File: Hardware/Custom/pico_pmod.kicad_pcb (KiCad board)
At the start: 2 copper layers, 50 x 37 mm, 44 parts, among them J1 Conn_02x06_Odd_Even, J2 Conn_02x06_Odd_Even, J3 Conn_02x06_Odd_Even, J4 USB_C_Receptacle_USB2.0, J5 Conn_01x04, SW1 SW_Push, SW2 SW_Push, U1 RP2040, U2 W25Q128JVS, U3 NCP1117-3.3_SOT223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

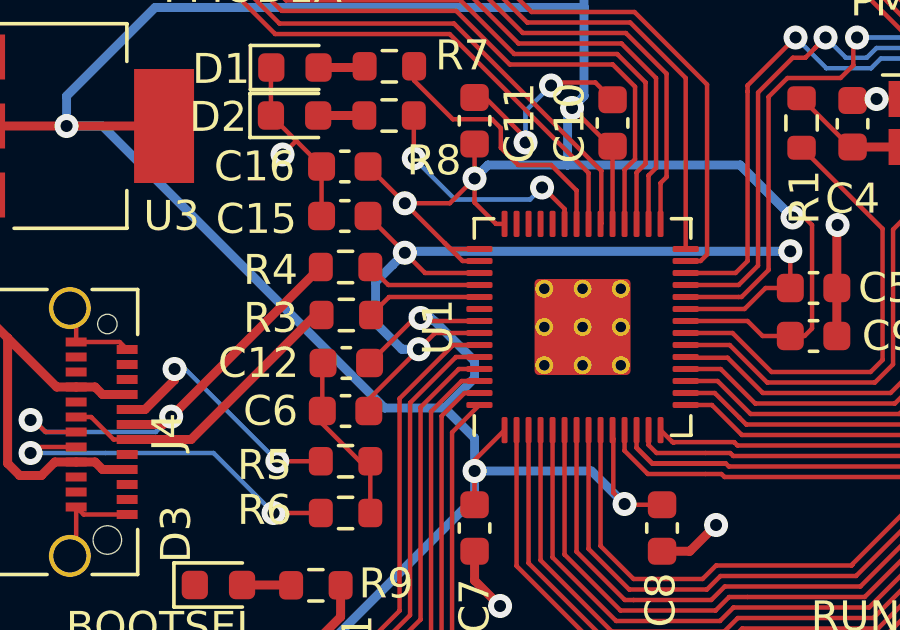
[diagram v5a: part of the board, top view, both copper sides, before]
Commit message: Ensure that pins 48 and 49 are connected to 3v3
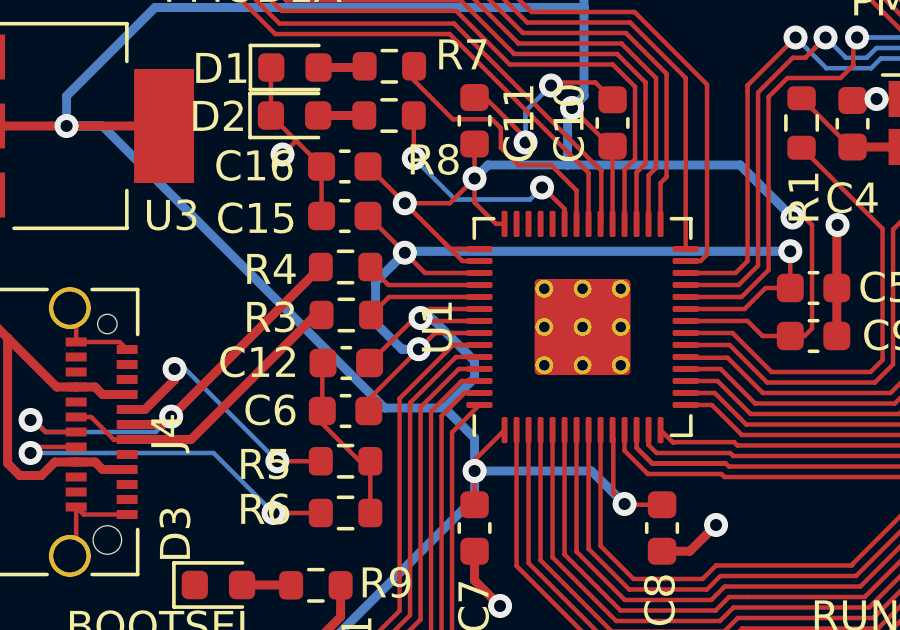
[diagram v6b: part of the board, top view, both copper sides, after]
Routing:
- net +3V3: track 200.0 -> 202.6 mm
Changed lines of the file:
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@@
     (thickness 1.6)
     (drawings 24)
-    (tracks 783)
+    (tracks 787)
     (zones 0)
     (modules 44)
@@
   (page A4)
   (layers
-    (0 F.Cu signal)
+    (0 F.Cu signal hide)
     (31 B.Cu signal)
     (32 B.Adhes user)
@@
   (segment (start 143.175 71.175) (end 144 70.35) (width 0.15) (layer F.Cu) (net 2))
   (segment (start 141.675 71.175) (end 143.175 71.175) (width 0.15) (layer F.Cu) (net 2))
+  (segment (start 142.5 74.7) (end 142.2 75) (width 0.15) (layer F.Cu) (net 2))
+  (segment (start 144.1625 74.7) (end 142.5 74.7) (width 0.15) (layer F.Cu) (net 2))
+  (segment (start 142.55 75) (end 142.65 75.1) (width 0.15) (layer B.Cu) (net 2))
+  (segment (start 142.2 75) (end 142.55 75) (width 0.15) (layer B.Cu) (net 2))
   (segment (start 160.75 67.75) (end 160.7 67.7) (width 0.3) (layer F.Cu) (net 3))
   (segment (start 162.7 67.75) (end 160.75 67.75) (width 0.3) (layer F.Cu) (net 3))

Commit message: update resistor values from schimatic
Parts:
- R7, R8, R9: value R -> 330
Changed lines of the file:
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@@
       (effects (font (size 1 1) (thickness 0.15)))
     )
-    (fp_text value R (at 0 1.43) (layer F.Fab) hide
+    (fp_text value 330 (at 0 1.43) (layer F.Fab) hide
       (effects (font (size 1 1) (thickness 0.15)))
     )
@@
       (effects (font (size 1 1) (thickness 0.15)))
     )
-    (fp_text value R (at 0 1.43) (layer F.Fab) hide
+    (fp_text value 330 (at 0 1.43) (layer F.Fab) hide
       (effects (font (size 1 1) (thickness 0.15)))
     )
@@
       (effects (font (size 1 1) (thickness 0.15)))
     )
-    (fp_text value R (at 0 1.43) (layer F.Fab) hide
+    (fp_text value 330 (at 0 1.43) (layer F.Fab) hide
       (effects (font (size 1 1) (thickness 0.15)))
     )

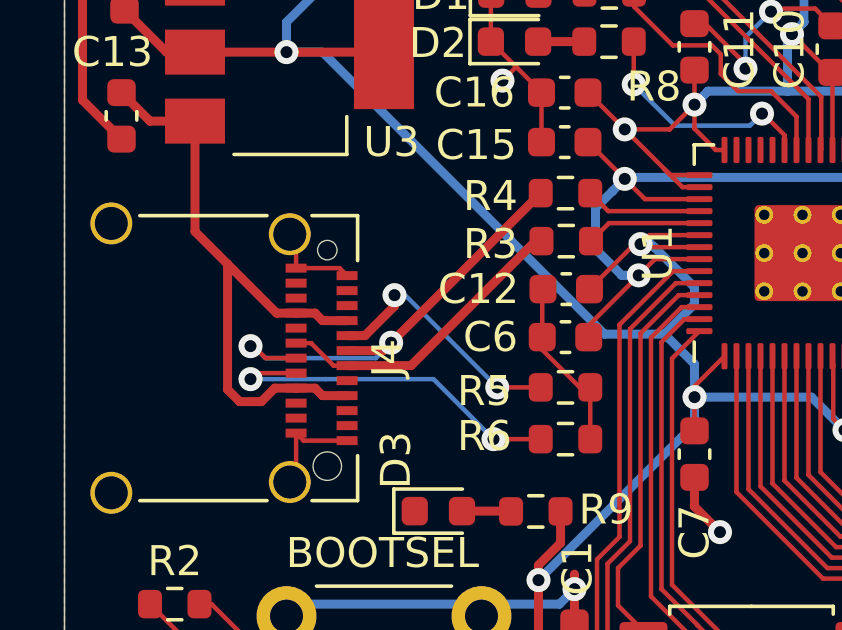
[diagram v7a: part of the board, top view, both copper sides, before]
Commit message: Correct USB DP and DN on PCB for #7
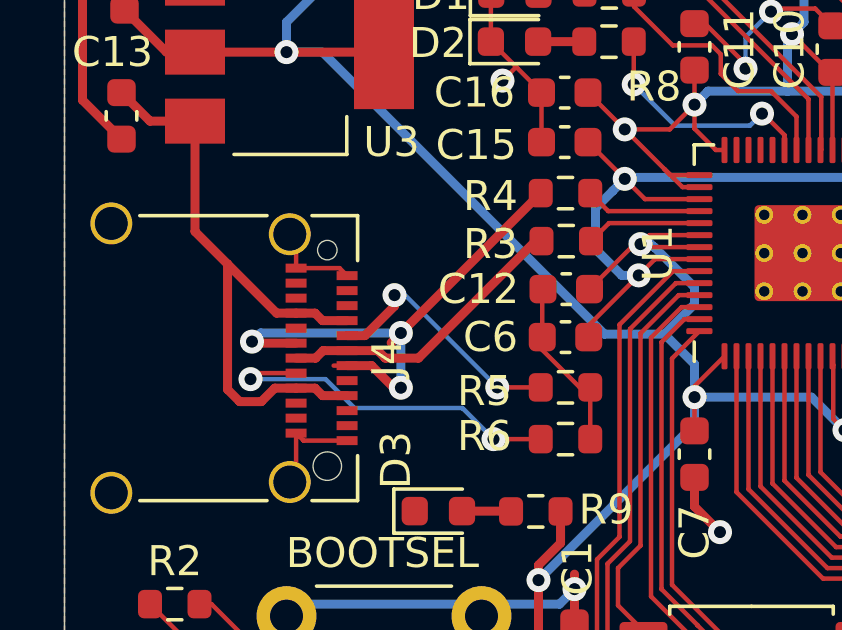
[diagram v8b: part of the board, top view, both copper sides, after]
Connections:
- J4 pad A7: USB_DN -> USB_DM
- J4 pad B7: USB_DN -> USB_DM
- R3 pad 1: USB_DN -> USB_DP
- R4 pad 1: USB_DP -> USB_DM
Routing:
- net USB_DM: track 0.00 -> 18.2 mm, vias 0 -> 3
- net USB_DN: track 10.2 -> 0.00 mm
- net USB_DP: track 15.4 -> 10.0 mm, vias 2 -> 0
